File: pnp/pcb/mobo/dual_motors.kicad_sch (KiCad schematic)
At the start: 9 parts, among them M5 MOTOR1, M6 MOTOR2

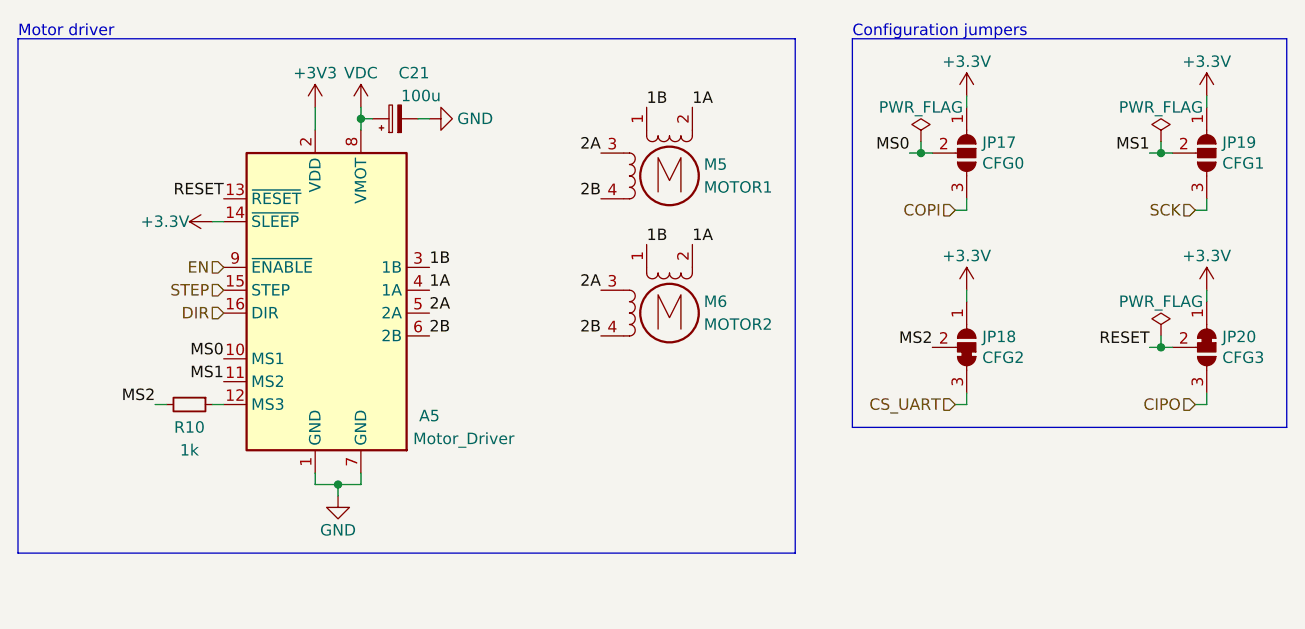
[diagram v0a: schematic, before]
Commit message: first commit of rev04 mobo beta 0. makes solder-selectable jumpers on back side of board not jumped to work with kit drivers, y2 motor port rotated correctly, moves traces out from underneath solder jumpers, adds 0 ohm jumpers to bypass the usb hub, adds 4 pin DIN connector for power, adds large decoupling cap on power supply input to decrease rippling, changes diode choice for 5v multiplexer to one already in the BOM, flips resistors on mos1 to be less confusing
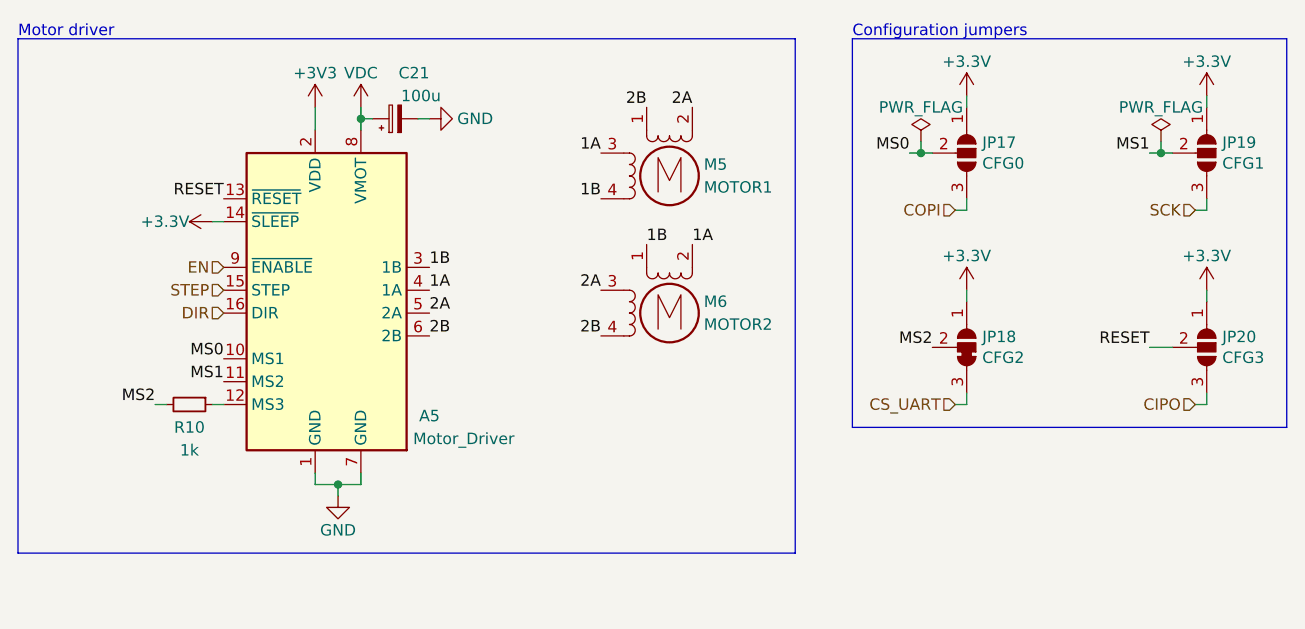
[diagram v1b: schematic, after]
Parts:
- removed JP20: CFG3, Jumper:SolderJumper-3_P1.3mm_Bridged12_RoundedPad1.0x1.5mm, symbol Jumper:SolderJumper_3_Bridged12
- added JP20: CFG3, Jumper:SolderJumper-3_P1.3mm_Open_RoundedPad1.0x1.5mm, symbol Jumper:SolderJumper_3_Open
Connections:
- net +3V3: now also JP20.1 (A)
- net 1A: now also M5.3; no longer M5.2 (-)
- net 1B: now also M5.4; no longer M5.1
- net 2A: now also M5.2 (-); no longer M5.3
- net 2B: now also M5.1; no longer M5.4
- net CIPO: now also JP20.3 (B)
- net RESET: now also JP20.2 (C)

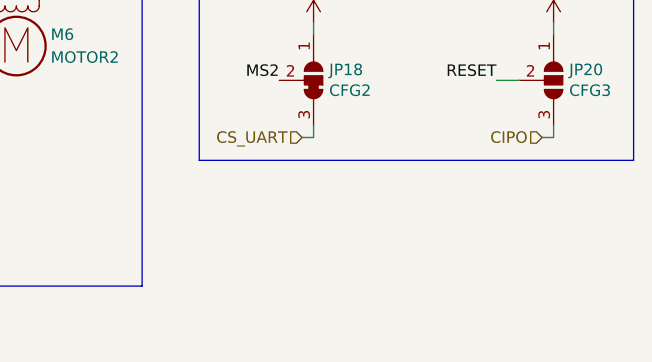
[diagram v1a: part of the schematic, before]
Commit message: another huge chunk of work on rev04 of the mobo. breaks out diag and index pin for TMC2209 sensorless homing. reduces unique part count by consolidating resistor values where possible. replaces full ADC pipeline with monolithic I2C vacuum sensor and an I2C multiplexer due to address collision issues with two sensors. adds solder selectable jumpers for selecting whether an axis uses switch or TMC homing. redoes lots of routing of the SPI lines up to the stepper drivers.
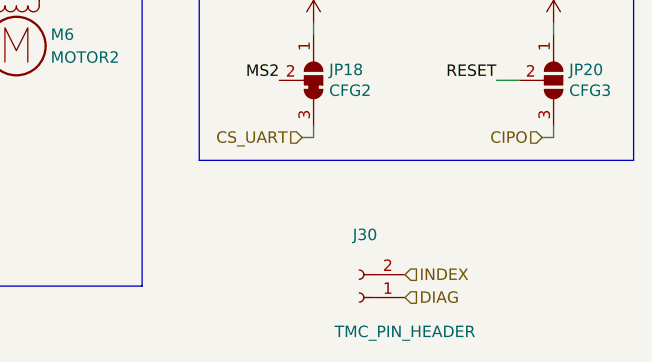
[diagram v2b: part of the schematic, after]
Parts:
- added J30: TMC_PIN_HEADER, Connector_PinHeader_2.54mm:PinHeader_1x02_P2.54mm_Vertical, symbol Connector:Conn_01x02_Female
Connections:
- new net DIAG: J30.1 (Pin_1)
- new net INDEX: J30.2 (Pin_2)
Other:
- company: (none) -> Opulo
- title: (none) -> LumenPnP Motherboard
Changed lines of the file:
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@@
   (paper "A4")
   (title_block
+    (title "LumenPnP Motherboard")
     (date "2022-03-29")
+    (company "Opulo")
   )
   (junction (at 119.38 127) (diameter 0) (color 0 0 0 0)
@@
     (effects (font (size 1.27 1.27)) (justify right))
   )
+  (hierarchical_label "DIAG" (shape input) (at 199.39 135.89 0)
+    (effects (font (size 1.27 1.27)) (justify left))
+  )
+  (hierarchical_label "INDEX" (shape input) (at 199.39 133.35 0)
+    (effects (font (size 1.27 1.27)) (justify left))
+  )
   (hierarchical_label "EN" (shape input) (at 106.68 102.87 180)
     (effects (font (size 1.27 1.27)) (justify right))
@@
   (symbol (lib_id "power:+3V3") (at 116.84 85.09 0)
     (in_bom yes) (on_board yes)
-    (property "Reference" "#PWR0227" (id 0) (at 116.84 88.9 0)
+    (property "Reference" "#PWR066" (id 0) (at 116.84 88.9 0)
       (effects (font (size 1.27 1.27)) hide)
     )
@@
   (symbol (lib_id "power:GND") (at 119.38 128.27 0)
     (in_bom yes) (on_board yes)
-    (property "Reference" "#PWR0225" (id 0) (at 119.38 134.62 0)
+    (property "Reference" "#PWR067" (id 0) (at 119.38 134.62 0)
       (effects (font (size 1.27 1.27)) hide)
     )
@@
   (symbol (lib_id "power:+3.3V") (at 105.41 97.79 90)
     (in_bom yes) (on_board yes)
-    (property "Reference" "#PWR0226" (id 0) (at 109.22 97.79 0)
+    (property "Reference" "#PWR065" (id 0) (at 109.22 97.79 0)
       (effects (font (size 1.27 1.27)) hide)
     )
@@
   (symbol (lib_id "power:VDC") (at 121.92 85.09 0)
     (in_bom yes) (on_board yes)
-    (property "Reference" "#PWR0228" (id 0) (at 121.92 87.63 0)
+    (property "Reference" "#PWR068" (id 0) (at 121.92 87.63 0)
       (effects (font (size 1.27 1.27)) hide)
     )
@@
   (symbol (lib_id "power:GND") (at 129.54 86.36 90)
     (in_bom yes) (on_board yes)
-    (property "Reference" "#PWR0229" (id 0) (at 135.89 86.36 0)
+    (property "Reference" "#PWR072" (id 0) (at 135.89 86.36 0)
       (effects (font (size 1.27 1.27)) hide)
     )
@@
   (symbol (lib_id "power:+3.3V") (at 215.9 105.41 0)
     (in_bom yes) (on_board yes)
-    (property "Reference" "#PWR0221" (id 0) (at 215.9 109.22 0)
+    (property "Reference" "#PWR070" (id 0) (at 215.9 109.22 0)
       (effects (font (size 1.27 1.27)) hide)
     )
@@
   (symbol (lib_id "power:+3.3V") (at 189.23 83.82 0)
     (in_bom yes) (on_board yes)
-    (property "Reference" "#PWR0223" (id 0) (at 189.23 87.63 0)
+    (property "Reference" "#PWR063" (id 0) (at 189.23 87.63 0)
       (effects (font (size 1.27 1.27)) hide)
     )
@@
   (symbol (lib_id "power:+3.3V") (at 215.9 83.82 0)
     (in_bom yes) (on_board yes)
-    (property "Reference" "#PWR0222" (id 0) (at 215.9 87.63 0)
+    (property "Reference" "#PWR069" (id 0) (at 215.9 87.63 0)
       (effects (font (size 1.27 1.27)) hide)
     )
@@
   (symbol (lib_id "power:+3.3V") (at 189.23 105.41 0)
     (in_bom yes) (on_board yes)
-    (property "Reference" "#PWR0224" (id 0) (at 189.23 109.22 0)
+    (property "Reference" "#PWR064" (id 0) (at 189.23 109.22 0)
       (effects (font (size 1.27 1.27)) hide)
     )
@@
   (symbol (lib_id "power:PWR_FLAG") (at 210.82 88.9 0)
     (in_bom yes) (on_board yes)
-    (property "Reference" "#FLG02" (id 0) (at 210.82 86.995 0)
+    (property "Reference" "#FLG06" (id 0) (at 210.82 86.995 0)
       (effects (font (size 1.27 1.27)) hide)
     )
@@
   (symbol (lib_id "power:PWR_FLAG") (at 184.15 88.9 0)
     (in_bom yes) (on_board yes)
-    (property "Reference" "#FLG01" (id 0) (at 184.15 86.995 0)
+    (property "Reference" "#FLG05" (id 0) (at 184.15 86.995 0)
       (effects (font (size 1.27 1.27)) hide)
     )
@@
     (pin "1")
   )
+  (symbol (lib_id "Connector:Conn_01x02_Female") (at 194.31 135.89 180)
+    (in_bom yes) (on_board yes)
+    (property "Reference" "J30" (id 0) (at 194.945 128.9263 0))
+    (property "Value" "TMC_PIN_HEADER" (id 1) (at 199.39 139.7 0))
+    (property "Footprint" "Connector_PinHeader_2.54mm:PinHeader_1x02_P2.54mm_Vertical" (id 2) (at 194.31 135.89 0)
+      (effects (font (size 1.27 1.27)) hide)
+    )
+    (property "Datasheet" "~" (id 3) (at 194.31 135.89 0)
+      (effects (font (size 1.27 1.27)) hide)
+    )
+    (pin "1")
+    (pin "2")
+  )
   (symbol (lib_id "Jumper:SolderJumper_3_Open") (at 215.9 111.76 270)

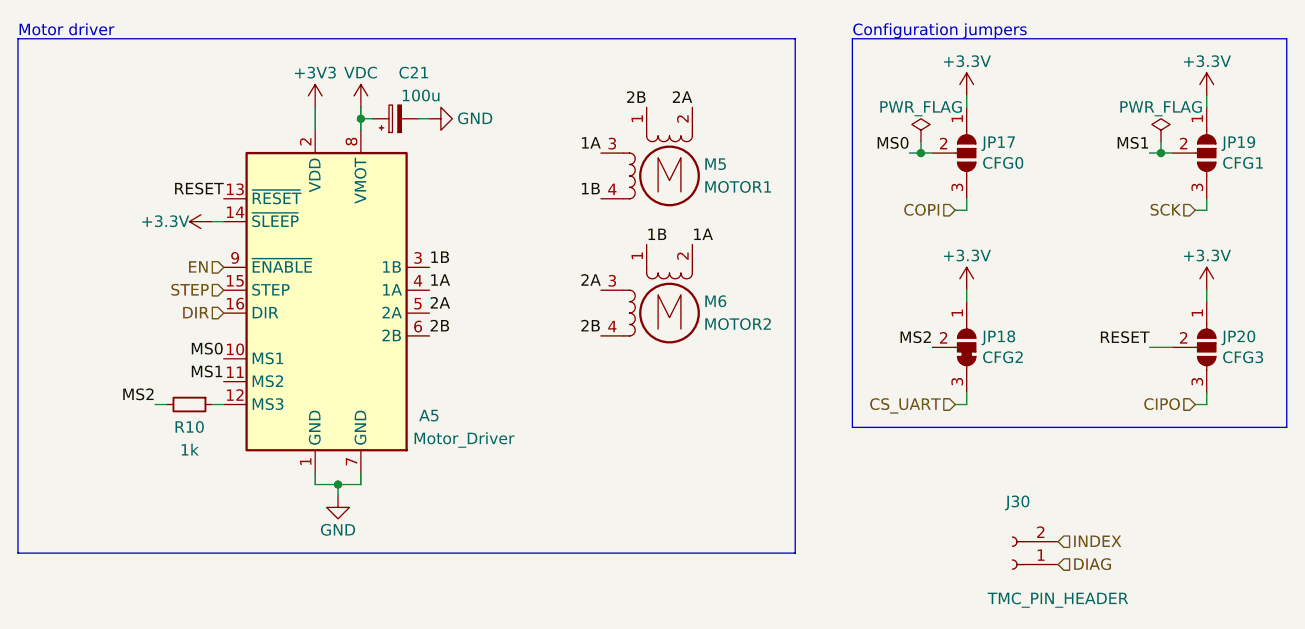
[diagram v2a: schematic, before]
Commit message: adds all missing 3d models, including custom model for the vacuum sensor. corrects wrong model for the diag and index pin header for the stepper drivers. changes the vacuum sensors to 3.3v power instead of 5v. cleans up some silkscreen.
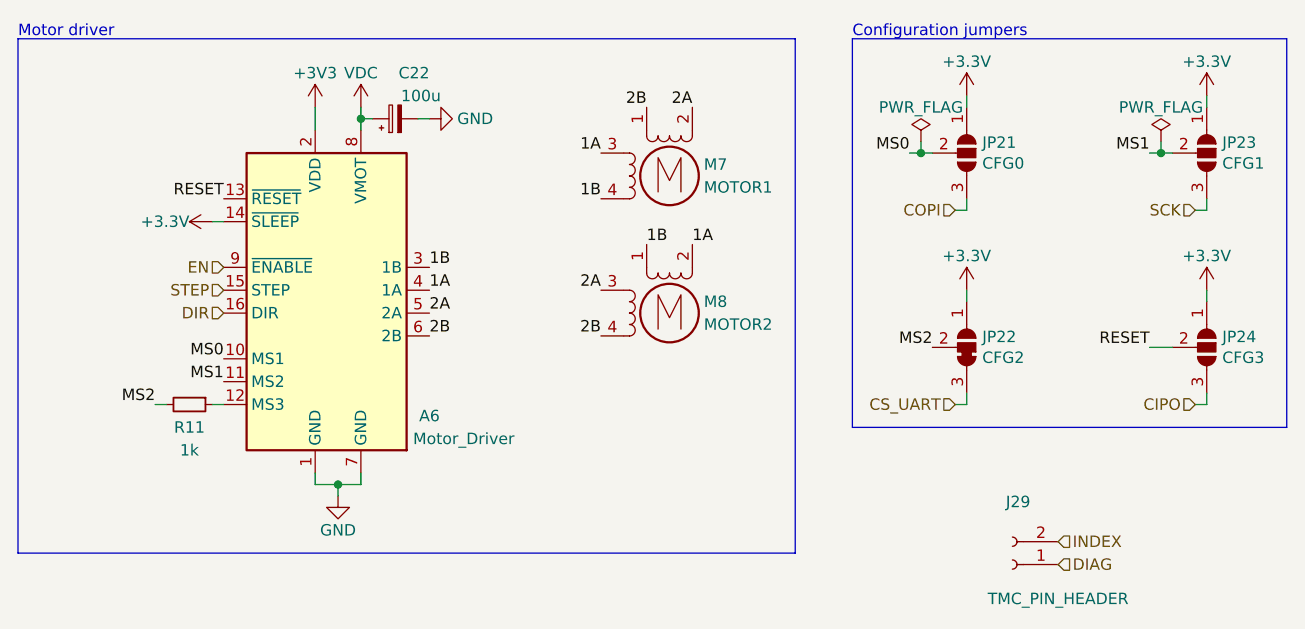
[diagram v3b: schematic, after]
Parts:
- J29: renamed from J30; footprint Connector_PinHeader_2.54mm:PinHeader_1x02_P2.54mm_Vertical -> Connector_PinSocket_2.54mm:PinSocket_1x02_P2.54mm_Vertical
- renumbered A5 to A6, C21 to C22, JP17 to JP21, JP18 to JP22, JP19 to JP23, JP20 to JP24, M5 to M7, M6 to M8, R10 to R11
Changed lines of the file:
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@@
   (symbol (lib_id "power:+3V3") (at 116.84 85.09 0)
     (in_bom yes) (on_board yes)
-    (property "Reference" "#PWR066" (id 0) (at 116.84 88.9 0)
+    (property "Reference" "#PWR0227" (id 0) (at 116.84 88.9 0)
       (effects (font (size 1.27 1.27)) hide)
     )
@@
   (symbol (lib_id "power:GND") (at 119.38 128.27 0)
     (in_bom yes) (on_board yes)
-    (property "Reference" "#PWR067" (id 0) (at 119.38 134.62 0)
+    (property "Reference" "#PWR0225" (id 0) (at 119.38 134.62 0)
       (effects (font (size 1.27 1.27)) hide)
     )
@@
   (symbol (lib_id "power:+3.3V") (at 105.41 97.79 90)
     (in_bom yes) (on_board yes)
-    (property "Reference" "#PWR065" (id 0) (at 109.22 97.79 0)
+    (property "Reference" "#PWR0226" (id 0) (at 109.22 97.79 0)
       (effects (font (size 1.27 1.27)) hide)
     )
@@
   (symbol (lib_id "Motor:Stepper_Motor_bipolar") (at 156.21 107.95 0)
     (in_bom yes) (on_board yes)
-    (property "Reference" "M6" (id 0) (at 160.02 106.68 0)
+    (property "Reference" "M8" (id 0) (at 160.02 106.68 0)
       (effects (font (size 1.27 1.27)) (justify left))
     )
@@
   (symbol (lib_id "Motor:Stepper_Motor_bipolar") (at 156.21 92.71 0)
     (in_bom yes) (on_board yes)
-    (property "Reference" "M5" (id 0) (at 160.02 91.44 0)
+    (property "Reference" "M7" (id 0) (at 160.02 91.44 0)
       (effects (font (size 1.27 1.27)) (justify left))
     )
@@
   (symbol (lib_id "Driver_Motor:Pololu_Breakout_A4988") (at 116.84 105.41 0)
     (in_bom yes) (on_board yes)
-    (property "Reference" "A5" (id 0) (at 129.54 119.38 0))
+    (property "Reference" "A6" (id 0) (at 129.54 119.38 0))
     (property "Value" "Motor_Driver" (id 1) (at 133.35 121.92 0))
     (property "Footprint" "Module:Pololu_Breakout-16_15.2x20.3mm" (id 2) (at 123.825 124.46 0)
@@
   (symbol (lib_id "power:VDC") (at 121.92 85.09 0)
     (in_bom yes) (on_board yes)
-    (property "Reference" "#PWR068" (id 0) (at 121.92 87.63 0)
+    (property "Reference" "#PWR0228" (id 0) (at 121.92 87.63 0)
       (effects (font (size 1.27 1.27)) hide)
     )
@@
   (symbol (lib_id "Device:C_Polarized_Small") (at 125.73 86.36 90)
     (in_bom yes) (on_board yes)
-    (property "Reference" "C21" (id 0) (at 129.54 81.28 90)
+    (property "Reference" "C22" (id 0) (at 129.54 81.28 90)
       (effects (font (size 1.27 1.27)) (justify left))
     )
@@
   (symbol (lib_id "power:GND") (at 129.54 86.36 90)
     (in_bom yes) (on_board yes)
-    (property "Reference" "#PWR072" (id 0) (at 135.89 86.36 0)
+    (property "Reference" "#PWR0229" (id 0) (at 135.89 86.36 0)
       (effects (font (size 1.27 1.27)) hide)
     )
@@
   (symbol (lib_id "power:+3.3V") (at 215.9 105.41 0)
     (in_bom yes) (on_board yes)
-    (property "Reference" "#PWR070" (id 0) (at 215.9 109.22 0)
+    (property "Reference" "#PWR0221" (id 0) (at 215.9 109.22 0)
       (effects (font (size 1.27 1.27)) hide)
     )
@@
   (symbol (lib_id "power:+3.3V") (at 189.23 83.82 0)
     (in_bom yes) (on_board yes)
-    (property "Reference" "#PWR063" (id 0) (at 189.23 87.63 0)
+    (property "Reference" "#PWR0223" (id 0) (at 189.23 87.63 0)
       (effects (font (size 1.27 1.27)) hide)
     )
@@
   (symbol (lib_id "power:+3.3V") (at 215.9 83.82 0)
     (in_bom yes) (on_board yes)
-    (property "Reference" "#PWR069" (id 0) (at 215.9 87.63 0)
+    (property "Reference" "#PWR0222" (id 0) (at 215.9 87.63 0)
       (effects (font (size 1.27 1.27)) hide)
     )
@@
   (symbol (lib_id "power:+3.3V") (at 189.23 105.41 0)
     (in_bom yes) (on_board yes)
-    (property "Reference" "#PWR064" (id 0) (at 189.23 109.22 0)
+    (property "Reference" "#PWR0224" (id 0) (at 189.23 109.22 0)
       (effects (font (size 1.27 1.27)) hide)
     )
@@
   (symbol (lib_id "Jumper:SolderJumper_3_Open") (at 189.23 90.17 270)
     (in_bom yes) (on_board yes)
-    (property "Reference" "JP17" (id 0) (at 190.9572 89.0016 90)
+    (property "Reference" "JP21" (id 0) (at 190.9572 89.0016 90)
       (effects (font (size 1.27 1.27)) (justify left))
     )
@@
   (symbol (lib_id "Jumper:SolderJumper_3_Open") (at 215.9 90.17 270)
     (in_bom yes) (on_board yes)
-    (property "Reference" "JP19" (id 0) (at 217.6272 89.0016 90)
+    (property "Reference" "JP23" (id 0) (at 217.6272 89.0016 90)
       (effects (font (size 1.27 1.27)) (justify left))
     )
@@
   (symbol (lib_id "Device:R_Small") (at 102.87 118.11 270)
     (in_bom yes) (on_board yes)
-    (property "Reference" "R10" (id 0) (at 102.87 120.65 90))
+    (property "Reference" "R11" (id 0) (at 102.87 120.65 90))
     (property "Value" "1k" (id 1) (at 102.87 123.19 90))
     (property "Footprint" "Resistor_SMD:R_0805_2012Metric" (id 2) (at 102.87 116.332 90)
@@
   (symbol (lib_id "index:SolderJumper_3_Bridged23") (at 189.23 111.76 270) (mirror x)
     (in_bom yes) (on_board yes)
-    (property "Reference" "JP18" (id 0) (at 190.9572 110.5916 90)
+    (property "Reference" "JP22" (id 0) (at 190.9572 110.5916 90)
       (effects (font (size 1.27 1.27)) (justify left))
     )
@@
   (symbol (lib_id "power:PWR_FLAG") (at 210.82 88.9 0)
     (in_bom yes) (on_board yes)
-    (property "Reference" "#FLG06" (id 0) (at 210.82 86.995 0)
+    (property "Reference" "#FLG02" (id 0) (at 210.82 86.995 0)
       (effects (font (size 1.27 1.27)) hide)
     )
@@
   (symbol (lib_id "power:PWR_FLAG") (at 184.15 88.9 0)
     (in_bom yes) (on_board yes)
-    (property "Reference" "#FLG05" (id 0) (at 184.15 86.995 0)
+    (property "Reference" "#FLG01" (id 0) (at 184.15 86.995 0)
       (effects (font (size 1.27 1.27)) hide)
     )
@@
   (symbol (lib_id "Connector:Conn_01x02_Female") (at 194.31 135.89 180)
     (in_bom yes) (on_board yes)
-    (property "Reference" "J30" (id 0) (at 194.945 128.9263 0))
+    (property "Reference" "J29" (id 0) (at 194.945 128.9263 0))
     (property "Value" "TMC_PIN_HEADER" (id 1) (at 199.39 139.7 0))
-    (property "Footprint" "Connector_PinHeader_2.54mm:PinHeader_1x02_P2.54mm_Vertical" (id 2) (at 194.31 135.89 0)
+    (property "Footprint" "Connector_PinSocket_2.54mm:PinSocket_1x02_P2.54mm_Vertical" (id 2) (at 194.31 135.89 0)
       (effects (font (size 1.27 1.27)) hide)
     )
@@
   (symbol (lib_id "Jumper:SolderJumper_3_Open") (at 215.9 111.76 270)
     (in_bom yes) (on_board yes)
-    (property "Reference" "JP20" (id 0) (at 217.6272 110.5916 90)
-      (effects (font (size 1.27 1.27)) (justify left))
-    )
+    (property "Reference" "JP24" (id 0) (at 217.6272 110.5916 90)
+      (effects (font (size 1.27 1.27)) (justify left))
+    )

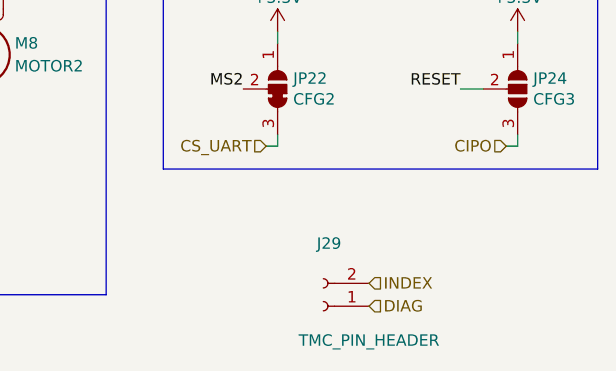
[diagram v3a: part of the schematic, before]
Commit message: fixes erc errors about pin connectivity
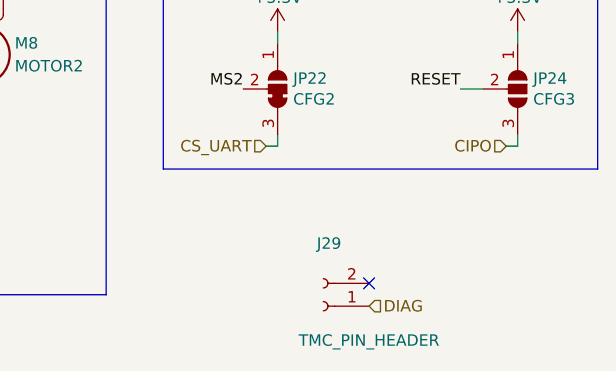
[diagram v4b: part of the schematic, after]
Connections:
- net INDEX: no longer names the net of J29.2 (Pin_2)
- no-connect marks 0 -> 1
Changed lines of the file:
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@@
   (junction (at 210.82 90.17) (diameter 0) (color 0 0 0 0)
   )
+  (no_connect (at 199.39 133.35))
   (polyline (pts (xy 83.82 77.47) (xy 83.82 134.62))
     (stroke (width 0) (type default) (color 0 0 0 0))
@@
     (effects (font (size 1.27 1.27)) (justify left))
   )
-  (hierarchical_label "INDEX" (shape input) (at 199.39 133.35 0)
-    (effects (font (size 1.27 1.27)) (justify left))
-  )
